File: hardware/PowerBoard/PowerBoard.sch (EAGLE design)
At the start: 134 parts, among them J1 CON-HRS-DM3AT, J2 CON-ZX62R-B-5P, J3 CON-FTSH-105-01-L-DV-K, J4 CON-S2B-PH-SM4-TB, J5 CON-PJ-102A, J6 CON-71741-0002-TOP, M1 MOUNT-HOLE3.3, M2 MOUNT-HOLE3.3, M3 MOUNT-HOLE3.3, M4 MOUNT-HOLE3.3, M5 FIDUCIAL1X2, M6 FIDUCIAL1X2, M7 FIDUCIAL1X2, M8 FIDUCIAL1X2, Q1 SI2323CDS, Q2 SI2312CDS, Q3 SI2333CDS, Q4 SI2333CDS, SW1 SWITCH-SPST, SW2 SWITCH-MS12ASG30, SW3 SWITCH-KSC-201J, U1 LTC4361-2DC, U10 MAX9938FEUK, U11 MAX9938FEUK, U12 MAX9938FEUK, U13 STM32F10XCXT6, U14 LTC2942-1, U15 USBLC6-2, U2 LTC4085, U3 XC6220B331MR-G, U4 XC6220B331MR-G, U5 XC9236A15DMR-G, U6 MIC94043, U8 MAX9938FEUK, U9 MAX9938FEUK, X1 ECX-2236, X2 ECX-31B

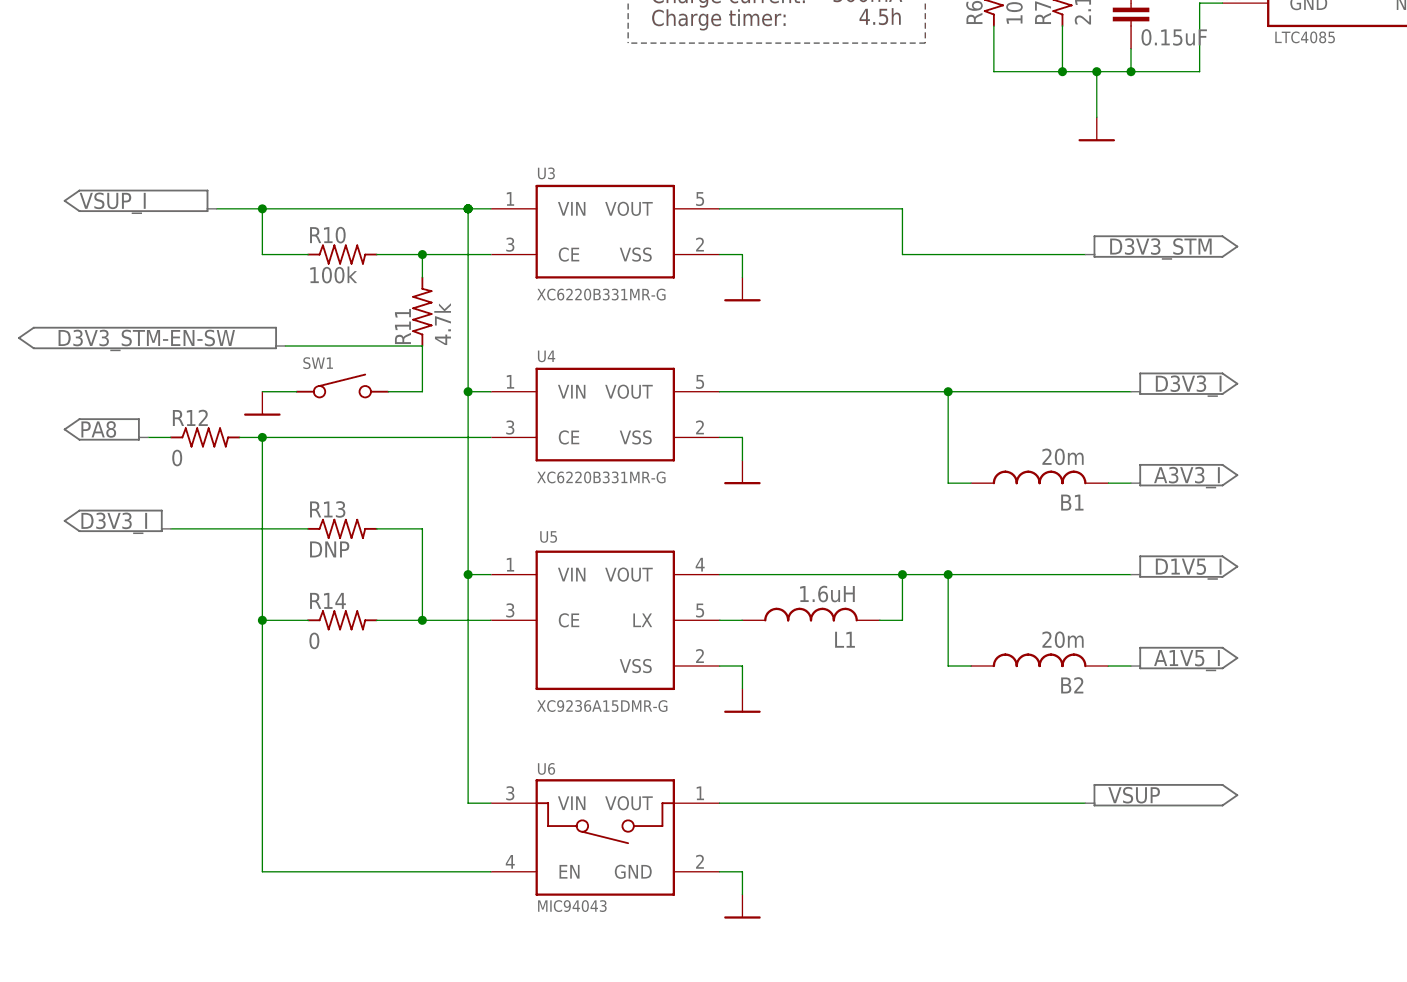
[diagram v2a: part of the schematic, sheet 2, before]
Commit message: - Minor changes in layout
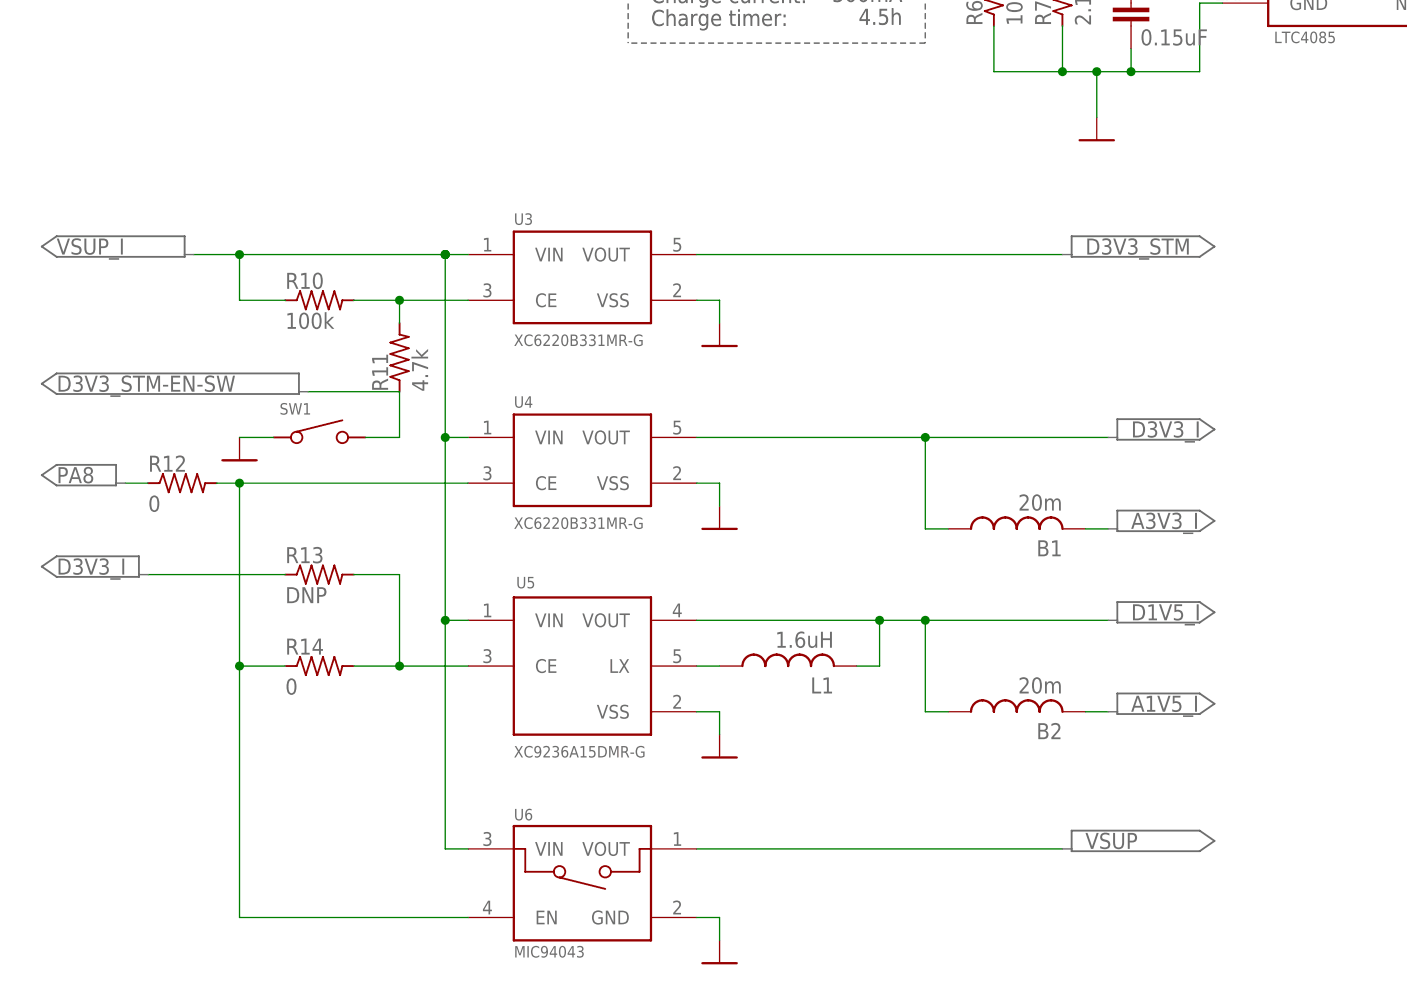
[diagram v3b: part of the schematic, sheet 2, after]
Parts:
- added R3, R54, R55, R56, R57: 0, powerboard:R0603
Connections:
- net AGND: now also R3.2, R54.2, R55.2, R56.2, R57.2
- net DGND: now also R3.1, R54.1, R55.1, R56.1, R57.1
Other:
- moved on the sheet: B1, B2, L1, R10, R11, R12, R13, R14, R45, SW1, U3, U4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

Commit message: - Layout update
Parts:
- removed R21, R48: 0, powerboard:R0603
- removed R51, R52: DNP, powerboard:R0603
- added TP14: TESTPOINT, powerboard:TESTPOINT-BLUE
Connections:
- removed net PA15-LED1: LED1.C, R21.2
- removed net PB4-SF: J6.25, R48.1
- net AGND: no longer R2.1, U10.GND, U10.GND@1, U8.GND, U8.GND@1, U9.GND, U9.GND@1
- net DGND: now also R2.1, U10.GND, U10.GND@1, U8.GND, U8.GND@1, U9.GND, U9.GND@1
- net JNTRST: no longer R52.1
- net JTDI: no longer R51.1
- net PA15: now also LED1.C; no longer R21.1, R51.2
- net PB5: now also J6.25; no longer R48.2, R52.2
- net VBUS: now also TP14.1
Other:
- note added: "South bridge"
- note removed: "West bridge"
- moved on the sheet: TP1, TP2, TP3

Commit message: - Layout update
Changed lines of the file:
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@@
 <part name="U$69" library="powerboard" deviceset="DGND" device=""/>
 <part name="U$70" library="powerboard" deviceset="DGND" device=""/>
+<part name="PORT65" library="powerboard" deviceset="PORT7" device=""/>
 </parts>
 <sheets>
@@
 <instance part="PORT84" gate="G$1" x="203.2" y="149.86"/>
 <instance part="PORT27" gate="G$1" x="20.32" y="71.12" rot="MR0"/>
+<instance part="PORT65" gate="G$1" x="43.18" y="30.48" rot="MR0"/>
 </instances>
 <busses>
@@
 <net name="D1V5-EN" class="0">
 <segment>
-<wire x1="53.34" y1="50.8" x2="58.42" y2="50.8" width="0.1524" layer="91"/>
-<wire x1="58.42" y1="50.8" x2="58.42" y2="40.64" width="0.1524" layer="91"/>
-<wire x1="58.42" y1="40.64" x2="66.04" y2="40.64" width="0.1524" layer="91"/>
-<wire x1="58.42" y1="40.64" x2="53.34" y2="40.64" width="0.1524" layer="91"/>
-<junction x="58.42" y="40.64"/>
+<wire x1="53.34" y1="50.8" x2="60.96" y2="50.8" width="0.1524" layer="91"/>
+<wire x1="60.96" y1="50.8" x2="60.96" y2="40.64" width="0.1524" layer="91"/>
+<wire x1="60.96" y1="40.64" x2="66.04" y2="40.64" width="0.1524" layer="91"/>
+<wire x1="60.96" y1="40.64" x2="53.34" y2="40.64" width="0.1524" layer="91"/>
+<junction x="60.96" y="40.64"/>
 <pinref part="R13" gate="G$1" pin="2"/>
 <pinref part="R14" gate="G$1" pin="2"/>
 <pinref part="U5" gate="G$1" pin="CE"/>
-</segment>
-</net>
+<wire x1="60.96" y1="40.64" x2="60.96" y2="30.48" width="0.1524" layer="91"/>
+<wire x1="60.96" y1="30.48" x2="58.42" y2="30.48" width="0.1524" layer="91"/>
+<label x="43.18" y="30.48" size="1.778" layer="95"/>
+</segment>
+</net>
